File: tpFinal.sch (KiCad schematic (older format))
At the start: 10 parts, among them P1 CONN_UART_TX_RX, P2 CONN_SPK, P3 CONN_PWR, P4 CONN_BAT, P5 CONN_SWD, U1 EMW3166

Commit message: Esquema corregido, PCB terminada
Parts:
- added FD1, FD2, FD3: Fiducial, Fiducial:Fiducial_1mm_Dia_2mm_Outer, symbol Mechanical:MountingHole
- added MH1, MH2, MH3, MH4: MountingHole_Pad, MountingHole:MountingHole_2.2mm_M2_Pad_Via, symbol Mechanical:MountingHole_Pad
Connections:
- net GND: now also MH1.1, MH2.1, MH3.1, MH4.1
- net cargadorDeBateria/V+ renamed +VDC
- no-connect marks 0 -> 6
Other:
- moved on the sheet: C10, R9

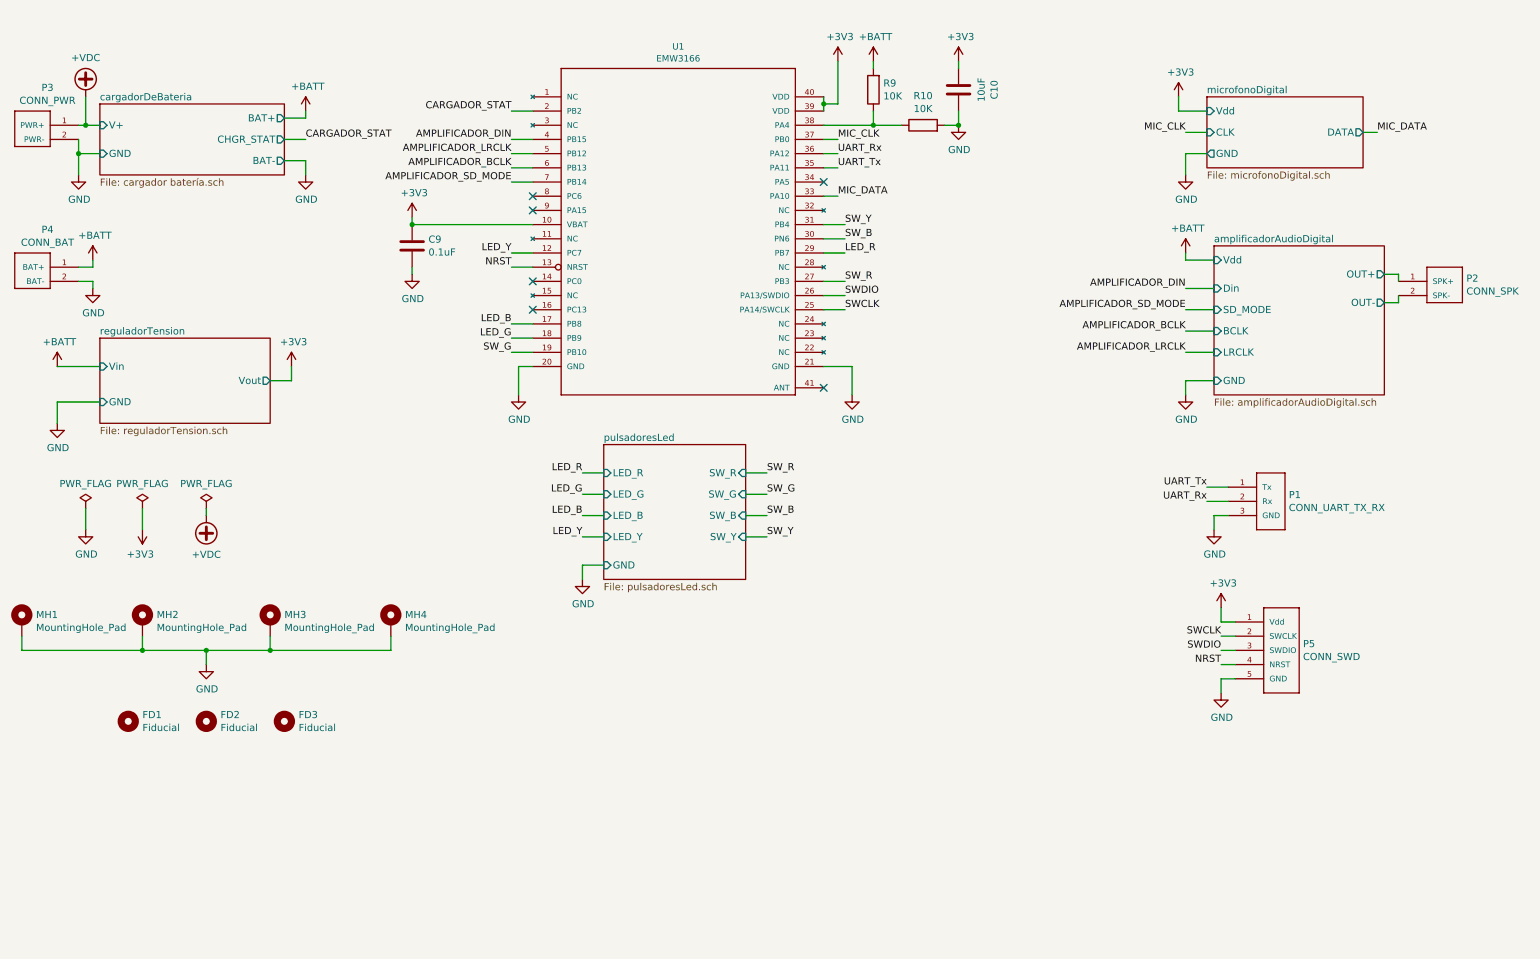
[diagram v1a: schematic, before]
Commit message: Se aplicaron correciones indicadas por el profesor en el esquemático
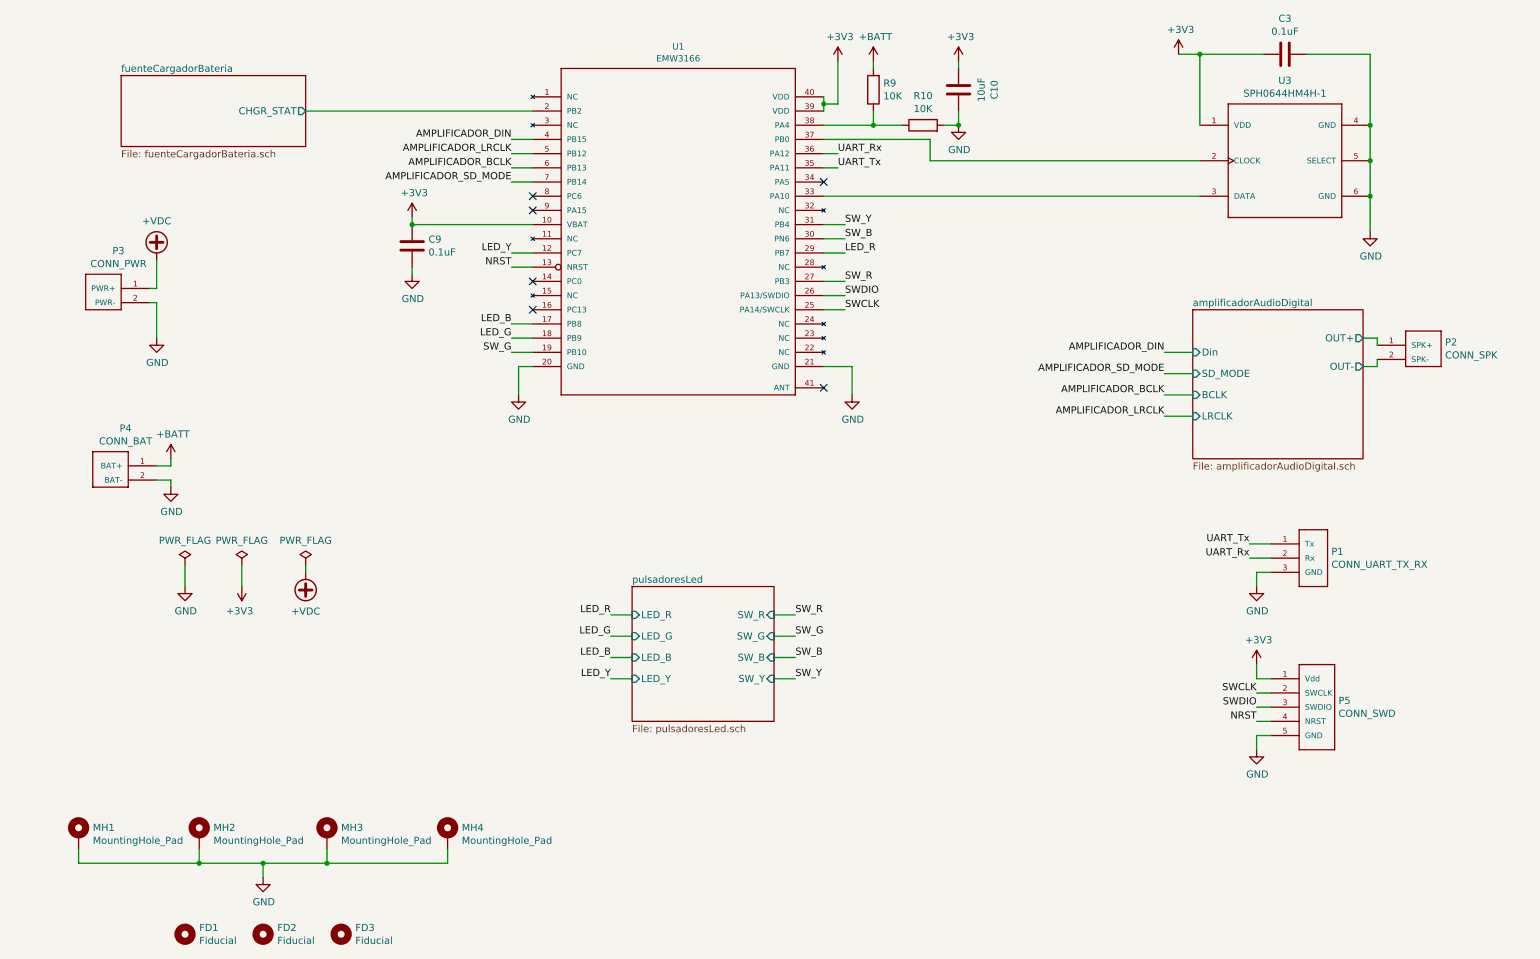
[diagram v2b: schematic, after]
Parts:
- added C3: 0.1uF, Capacitor_SMD:C_0805_2012Metric, symbol Device:C
- added U3: SPH0644HM4H-1, tpfinal:SPH0644HM4H-1, symbol tpfinal:SPH0644HM4H-1
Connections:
- net +3V3: now also C3.2, U3.1 (VDD)
- net GND: now also C3.1, U3.4 (GND), U3.5 (SELECT), U3.6 (GND)
- net CARGADOR_STAT renamed fuenteCargadorBateria/CHGR_STAT
- net MIC_CLK: no longer names the net of U1.37 (PB0)
- net MIC_CLK: now also U3.2 (CLOCK)
- net MIC_DATA: no longer names the net of U1.33 (PA10)
- net MIC_DATA: now also U3.3 (DATA)
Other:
- moved on the sheet: FD1, FD2, FD3, MH1, MH2, MH3, MH4, P1, P2, P3, P4, P5
